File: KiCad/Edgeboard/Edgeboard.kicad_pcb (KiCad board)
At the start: 2 copper layers, 20.3 x 81.3 mm, 4 parts, among them J2 Conn_02x25_Odd_Even

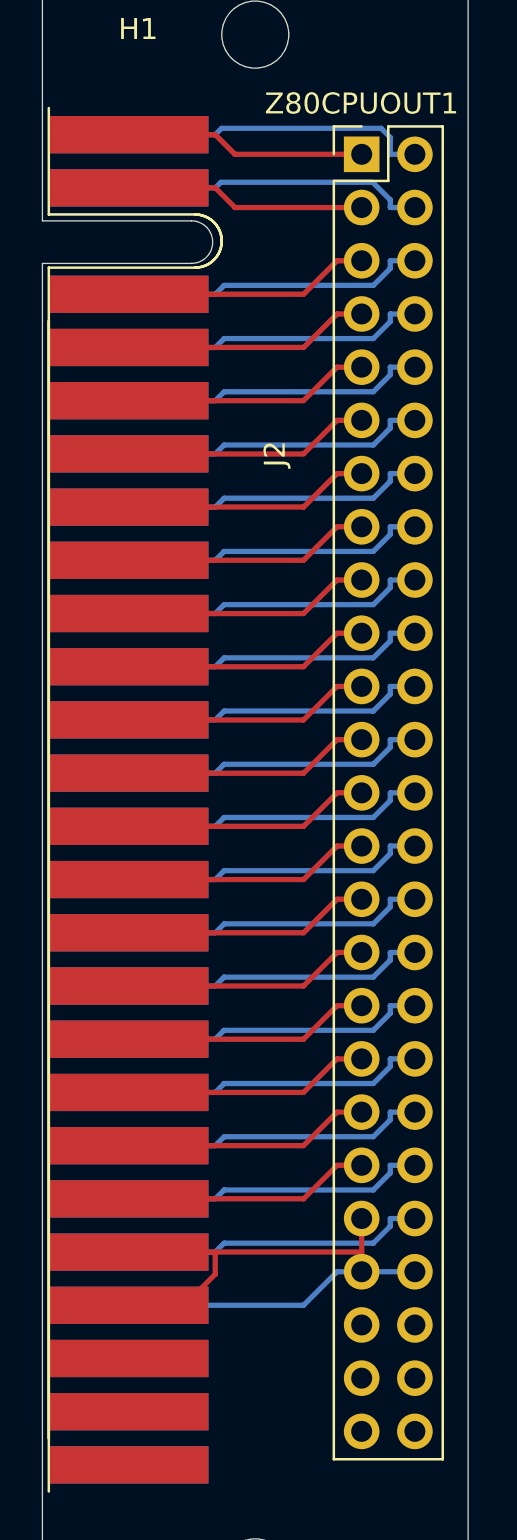
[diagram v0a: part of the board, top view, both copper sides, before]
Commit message: Improve EZ80,
Correct fault with layout of EdgeBoard. The test boards physically fitted old ACE add-ons but there was a mistake in the wiring.

Signed-off-by: John Bradley <flypie@rocketmail.com>
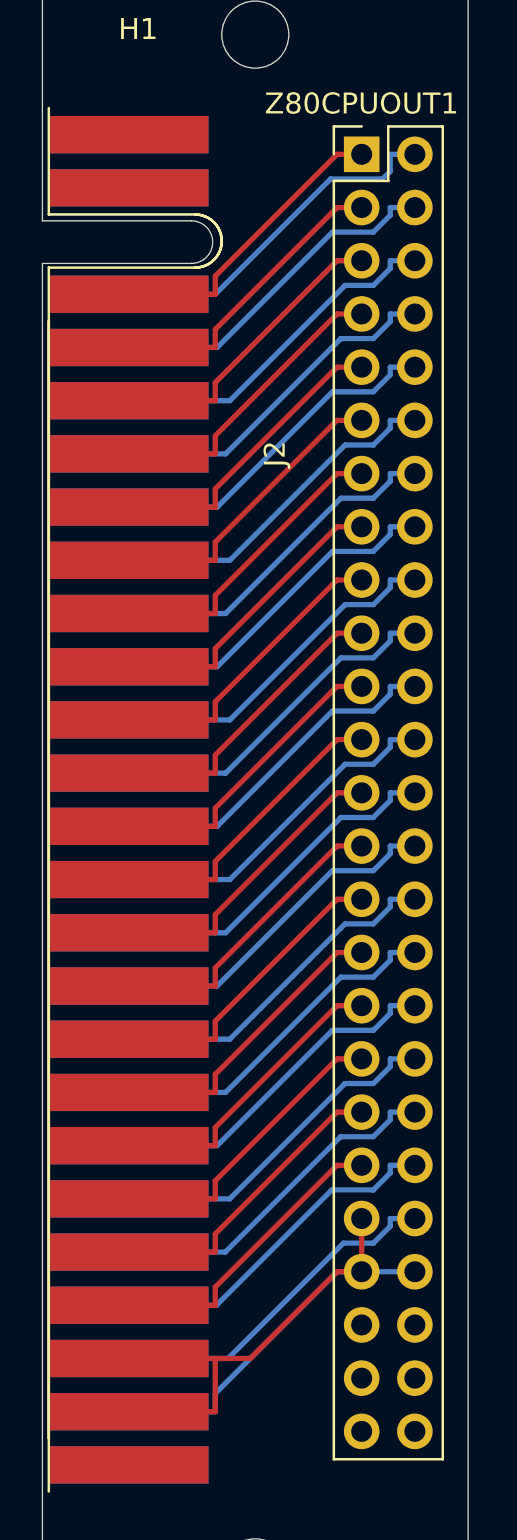
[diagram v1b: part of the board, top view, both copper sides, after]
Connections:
- J2 pad 1: /#WE -> Net-(J2-Pad1)
- J2 pad 10: /A3 -> /DA0
- J2 pad 11: /A8 -> /A0
- J2 pad 12: /A4 -> /A1
- J2 pad 13: /A9 -> /A7
- J2 pad 14: /A5 -> /A3
- J2 pad 15: /A10 -> /A8
- J2 pad 16: /A6 -> /A4
- J2 pad 17: /A2 -> /A9
- J2 pad 18: //REFSH -> /A5
- J2 pad 19: /DA5 -> /A10
- J2 pad 2: /DA7 -> Net-(J2-Pad2)
- J2 pad 20: //M1 -> /A6
- J2 pad 21: /DA3 -> /A2
- J2 pad 22: #RESET -> //REFSH
- J2 pad 23: /DA4 -> /DA5
- J2 pad 24: //BUSRQ -> //M1
- J2 pad 25: /A15 -> /DA3
- J2 pad 26: //WAIT -> #RESET
- J2 pad 27: /A14 -> /DA4
- J2 pad 28: //BUSAK -> //BUSRQ
- J2 pad 29: /A13 -> /A15
- J2 pad 3: /DA6 -> Net-(J2-Pad3)
- J2 pad 30: //WR -> //WAIT
- J2 pad 31: /A12 -> /A14
- J2 pad 32: //RD -> //BUSAK
- J2 pad 33: /A11 -> /A13
- J2 pad 34: //IOREQ -> //WR
- J2 pad 35: #CPUCLK -> /A12
- J2 pad 36: //MREQ -> //RD
- J2 pad 37: +5V -> /A11
- J2 pad 38: //HALT -> //IOREQ
- J2 pad 39: +9V -> #CPUCLK
- J2 pad 4: /DA2 -> Net-(J2-Pad4)
- J2 pad 40: #NMI -> //MREQ
- J2 pad 41: GND -> +5V
- J2 pad 42: #INT -> //HALT
- J2 pad 43: GND -> +9V
- J2 pad 44: GND -> #NMI
- J2 pad 45: Net-(J2-Pad45) -> GND
- J2 pad 46: Net-(J2-Pad46) -> #INT
- J2 pad 47: Net-(J2-Pad47) -> GND
- J2 pad 48: Net-(J2-Pad48) -> GND
- J2 pad 5: /DA1 -> /#WE
- J2 pad 6: /DA0 -> /DA7
- J2 pad 7: /A0 -> /DA6
- J2 pad 8: /A1 -> /DA2
- J2 pad 9: /A7 -> /DA1
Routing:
- net GND: track 33.8 -> 39.0 mm
- net /#WE: track 11.5 -> 14.4 mm
- net /DA6: track 11.5 -> 14.4 mm
- net /A8: track 11.8 -> 14.4 mm
- net /A13: track 11.8 -> 14.4 mm
- net /DA3: track 11.8 -> 14.4 mm
- net /A9: track 11.8 -> 14.4 mm
- net /A2: track 11.8 -> 14.4 mm
- net /A14: track 11.8 -> 14.4 mm
- net /A12: track 11.8 -> 14.4 mm
- net /A0: track 11.8 -> 14.4 mm
- net +9V: track 11.8 -> 14.4 mm
- net #CPUCLK: track 11.8 -> 14.4 mm
- net /DA5: track 11.8 -> 14.4 mm
- net /DA4: track 11.8 -> 14.4 mm
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
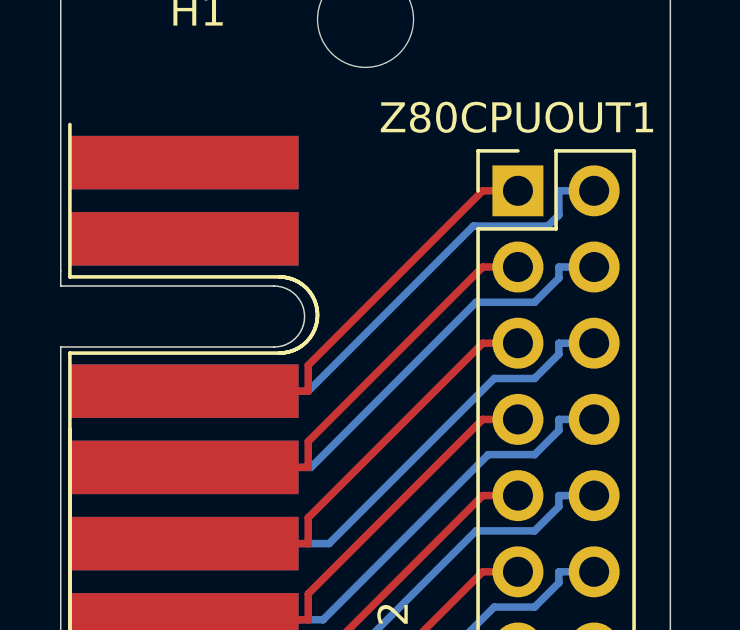
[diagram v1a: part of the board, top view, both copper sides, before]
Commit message: First complete system. Unlikely to work but will serve as the basis of a system to test VGA.
Signed-off-by: John Bradley <flypie@rocketmail.com>
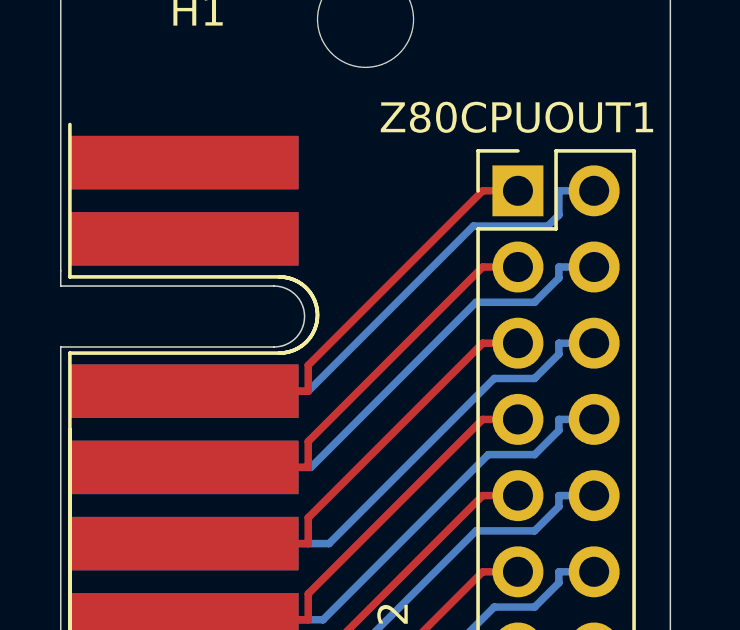
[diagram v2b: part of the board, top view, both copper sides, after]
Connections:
- net //BUSAK renamed //BUSAK
- net //BUSRQ renamed //BUSRQ
- net //HALT renamed //HALT
- net //IOREQ renamed //IOREQ
- net //M1 renamed //M1
- net //MREQ renamed //MREQ
- net //RD renamed //RD
- net //REFSH renamed //REFSH
- net //WAIT renamed //WAIT
- net //WR renamed //WR
- J2 pad 1: Net-(J2-Pad1) -> unconnected-(J2-Pad1)
- J2 pad 2: Net-(J2-Pad2) -> unconnected-(J2-Pad2)
- J2 pad 3: Net-(J2-Pad3) -> unconnected-(J2-Pad3)
- J2 pad 4: Net-(J2-Pad4) -> unconnected-(J2-Pad4)
- J2 pad 49: Net-(J2-Pad49) -> unconnected-(J2-Pad49)
- J2 pad 50: Net-(J2-Pad50) -> unconnected-(J2-Pad50)
- Z80CPUOUT1 pad 45: Net-(Z80CPUOUT1-Pad45) -> unconnected-(Z80CPUOUT1-Pad45)
- Z80CPUOUT1 pad 46: Net-(Z80CPUOUT1-Pad46) -> unconnected-(Z80CPUOUT1-Pad46)
- Z80CPUOUT1 pad 47: Net-(Z80CPUOUT1-Pad47) -> unconnected-(Z80CPUOUT1-Pad47)
- Z80CPUOUT1 pad 48: Net-(Z80CPUOUT1-Pad48) -> unconnected-(Z80CPUOUT1-Pad48)
- Z80CPUOUT1 pad 49: Net-(Z80CPUOUT1-Pad49) -> unconnected-(Z80CPUOUT1-Pad49)
- Z80CPUOUT1 pad 50: Net-(Z80CPUOUT1-Pad50) -> unconnected-(Z80CPUOUT1-Pad50)
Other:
- net class Default removed

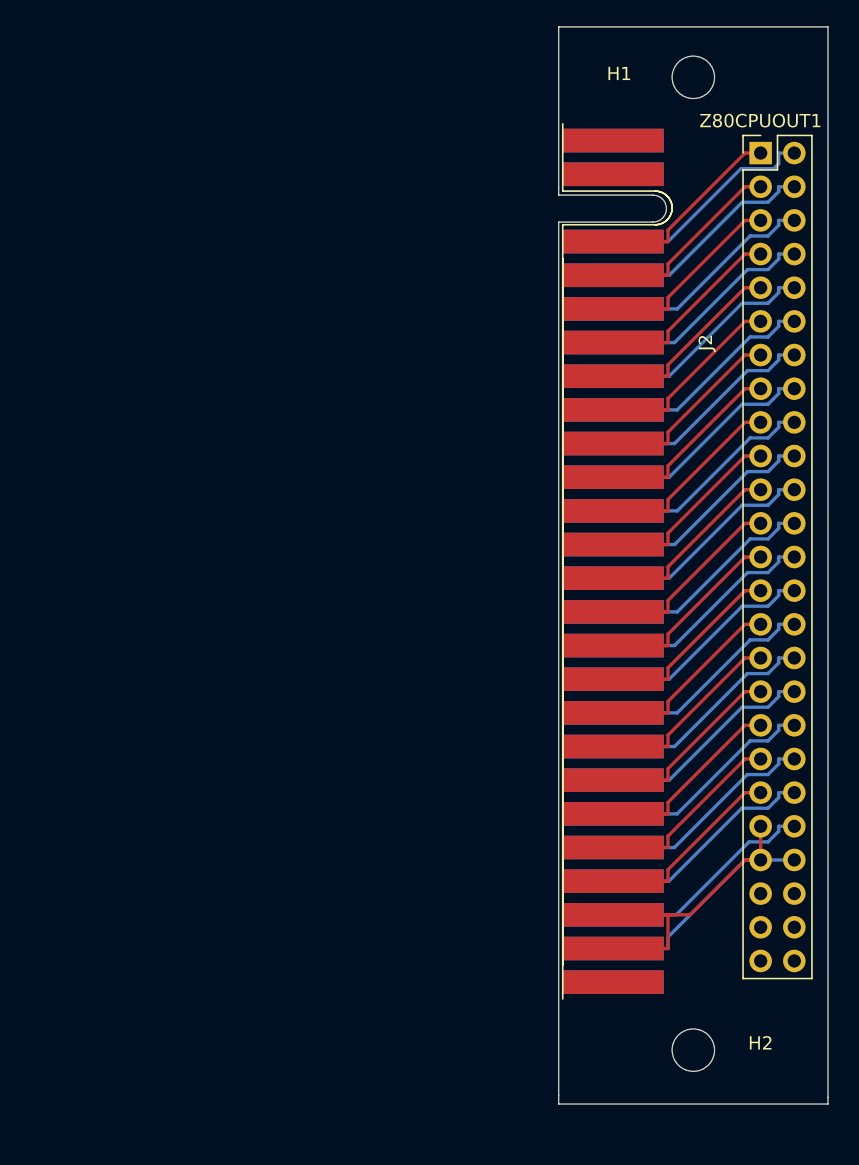
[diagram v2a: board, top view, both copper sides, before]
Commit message: Complete Move to KiCAD V6.
Plus various bits of ROM Dev and backups.

Signed-off-by: John Bradley <flypie@rocketmail.com>
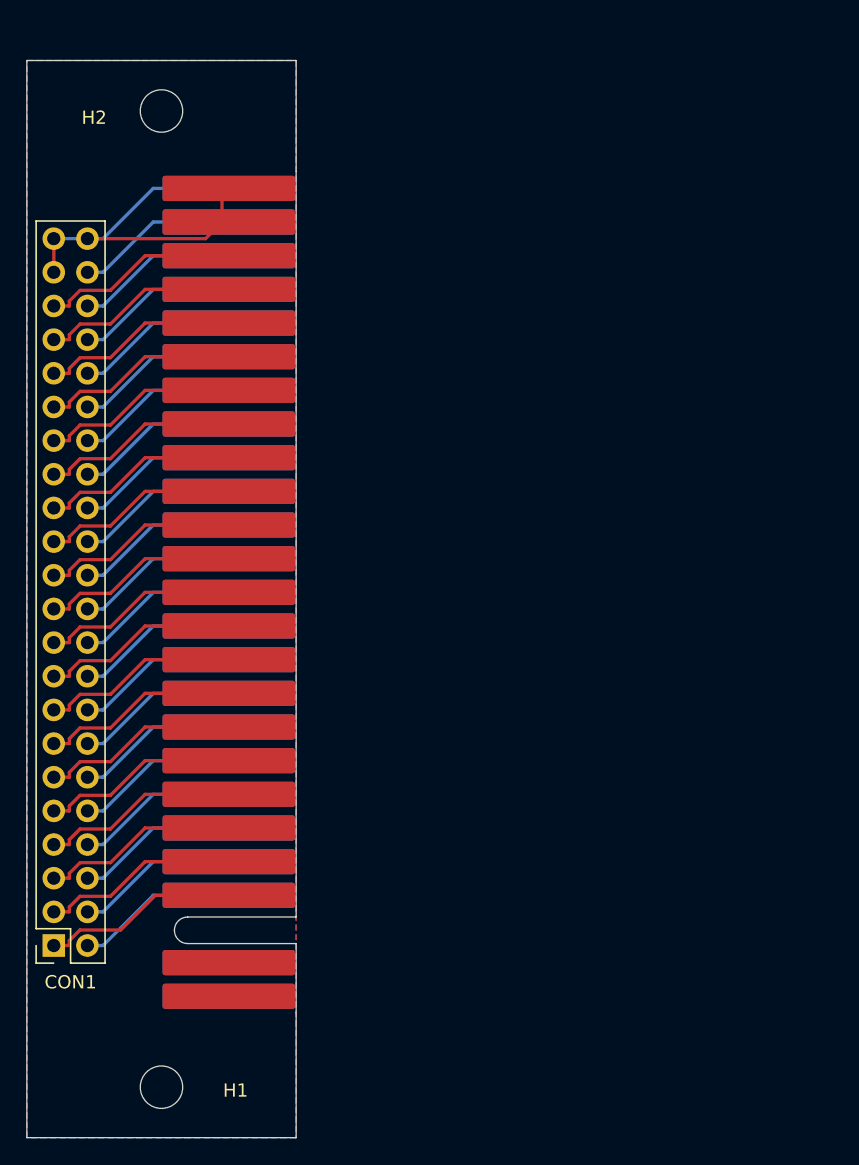
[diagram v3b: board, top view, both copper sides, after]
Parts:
- removed J2: Conn_02x25_Odd_Even, Connector_PCBEdge:JupiterAce
- removed Z80CPUOUT1: Conn_02x25_Odd_Even, Connector_PinHeader_2.54mm:PinHeader_2x25_P2.54mm_Vertical
- added CON1: EDG-CON-JA, Connector_PinSocket_2.54mm:PinSocket_2x22_P2.54mm_Vertical, F.Cu at (103.6, 117.6)
- added CON2: EDG-CON-JA, ExtraFootprints:EDG-CON-JA, F.Cu at (121.9, 122.7)
- moved H1 86.1 mm to (111.8, 128.3), turned to 180 degrees
- moved H2 81.4 mm to (111.8, 54.6), turned to 180 degrees
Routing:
- net /DA7: track 16.9 -> 0.00 mm
- net //IOREQ: track 16.6 -> 0.00 mm
- net //BUSRQ: track 16.6 -> 0.00 mm
- net #INT: track 16.6 -> 0.00 mm
- net //WR: track 16.6 -> 0.00 mm
- net //MREQ: track 16.6 -> 0.00 mm
- net //M1: track 16.6 -> 0.00 mm
- net //HALT: track 16.6 -> 0.00 mm
- net /DA0: track 16.6 -> 0.00 mm
- net //WAIT: track 16.6 -> 0.00 mm
- net //REFSH: track 16.6 -> 0.00 mm
- net //RD: track 16.6 -> 0.00 mm
- net //BUSAK: track 16.6 -> 0.00 mm
- net #NMI: track 16.6 -> 0.00 mm
- net /DA2: track 16.6 -> 0.00 mm
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- added copper zone on B.Cu, net GND
- added copper zone on F.Cu, net GND
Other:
- outline, holes or cut-outs redrawn
